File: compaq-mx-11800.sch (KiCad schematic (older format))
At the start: 246 parts

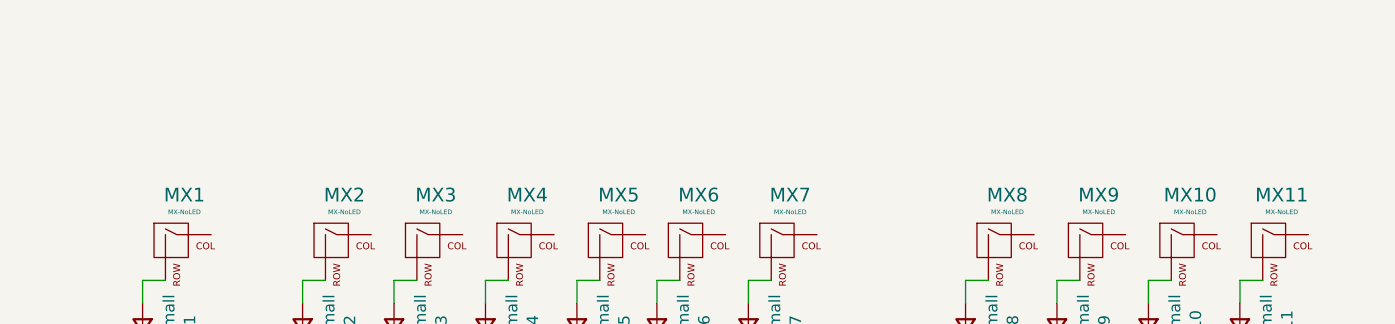
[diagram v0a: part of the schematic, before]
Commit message: add rest of the pcb mounting holes
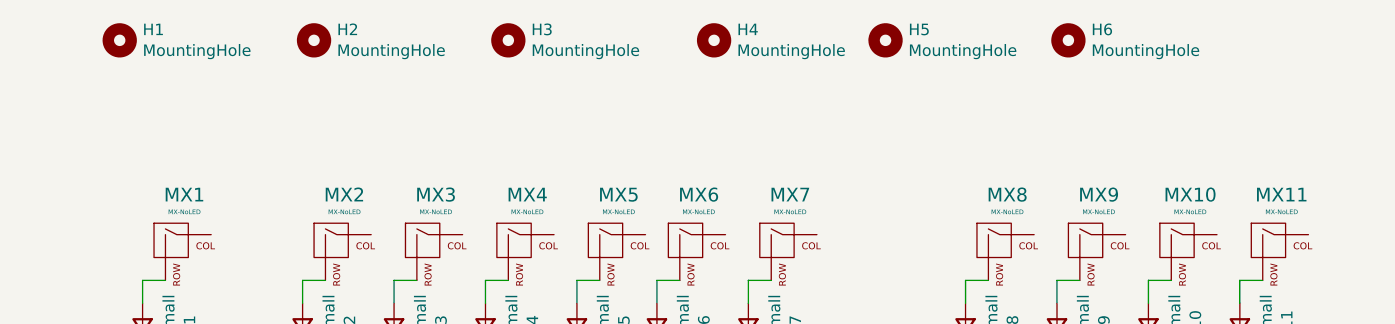
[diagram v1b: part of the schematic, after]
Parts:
- added H1, H2, H3, H4, H5: MountingHole, MountingHole:MountingHole_3.2mm_M3, symbol Mechanical:MountingHole
- added H6: MountingHole, Keebio-Parts:SolidCopper, symbol Mechanical:MountingHole
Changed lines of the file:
@@
+	1    0    0    -1
+$EndComp
+$Comp
+L Mechanical:MountingHole H1
+U 1 1 61C64BC8
+P 1000 100
+F 0 "H1" H 1100 146 50  0000 L CNN
+F 1 "MountingHole" H 1100 55  50  0000 L CNN
+F 2 "MountingHole:MountingHole_3.2mm_M3" H 1000 100 50  0001 C CNN
+F 3 "~" H 1000 100 50  0001 C CNN
+	1    1000 100
+	1    0    0    -1
+$EndComp
+$Comp
+L Mechanical:MountingHole H2
+U 1 1 61C9736A
+P 1850 100
+F 0 "H2" H 1950 146 50  0000 L CNN
+F 1 "MountingHole" H 1950 55  50  0000 L CNN
+F 2 "MountingHole:MountingHole_3.2mm_M3" H 1850 100 50  0001 C CNN
+F 3 "~" H 1850 100 50  0001 C CNN
+	1    1850 100
+	1    0    0    -1
+$EndComp
+$Comp
+L Mechanical:MountingHole H3
+U 1 1 61C97D62
+P 2700 100
+F 0 "H3" H 2800 146 50  0000 L CNN
+F 1 "MountingHole" H 2800 55  50  0000 L CNN
+F 2 "MountingHole:MountingHole_3.2mm_M3" H 2700 100 50  0001 C CNN
+F 3 "~" H 2700 100 50  0001 C CNN
+	1    2700 100
+	1    0    0    -1
+$EndComp
+$Comp
+L Mechanical:MountingHole H4
+U 1 1 61C98E0E
+P 3600 100
+F 0 "H4" H 3700 146 50  0000 L CNN
+F 1 "MountingHole" H 3700 55  50  0000 L CNN
+F 2 "MountingHole:MountingHole_3.2mm_M3" H 3600 100 50  0001 C CNN
+F 3 "~" H 3600 100 50  0001 C CNN
+	1    3600 100
+	1    0    0    -1
+$EndComp
+$Comp
+L Mechanical:MountingHole H5
+U 1 1 61CD4313
+P 4350 100
+F 0 "H5" H 4450 146 50  0000 L CNN
+F 1 "MountingHole" H 4450 55  50  0000 L CNN
+F 2 "MountingHole:MountingHole_3.2mm_M3" H 4350 100 50  0001 C CNN
+F 3 "~" H 4350 100 50  0001 C CNN
+	1    4350 100
+	1    0    0    -1
+$EndComp
+$Comp
+L Mechanical:MountingHole H6
+U 1 1 61D29BE7
+P 5150 100
+F 0 "H6" H 5250 146 50  0000 L CNN
+F 1 "MountingHole" H 5250 55  50  0000 L CNN
+F 2 "Keebio-Parts:SolidCopper" H 5150 100 50  0001 C CNN
+F 3 "~" H 5150 100 50  0001 C CNN
+	1    5150 100
 	1    0    0    -1
 $EndComp

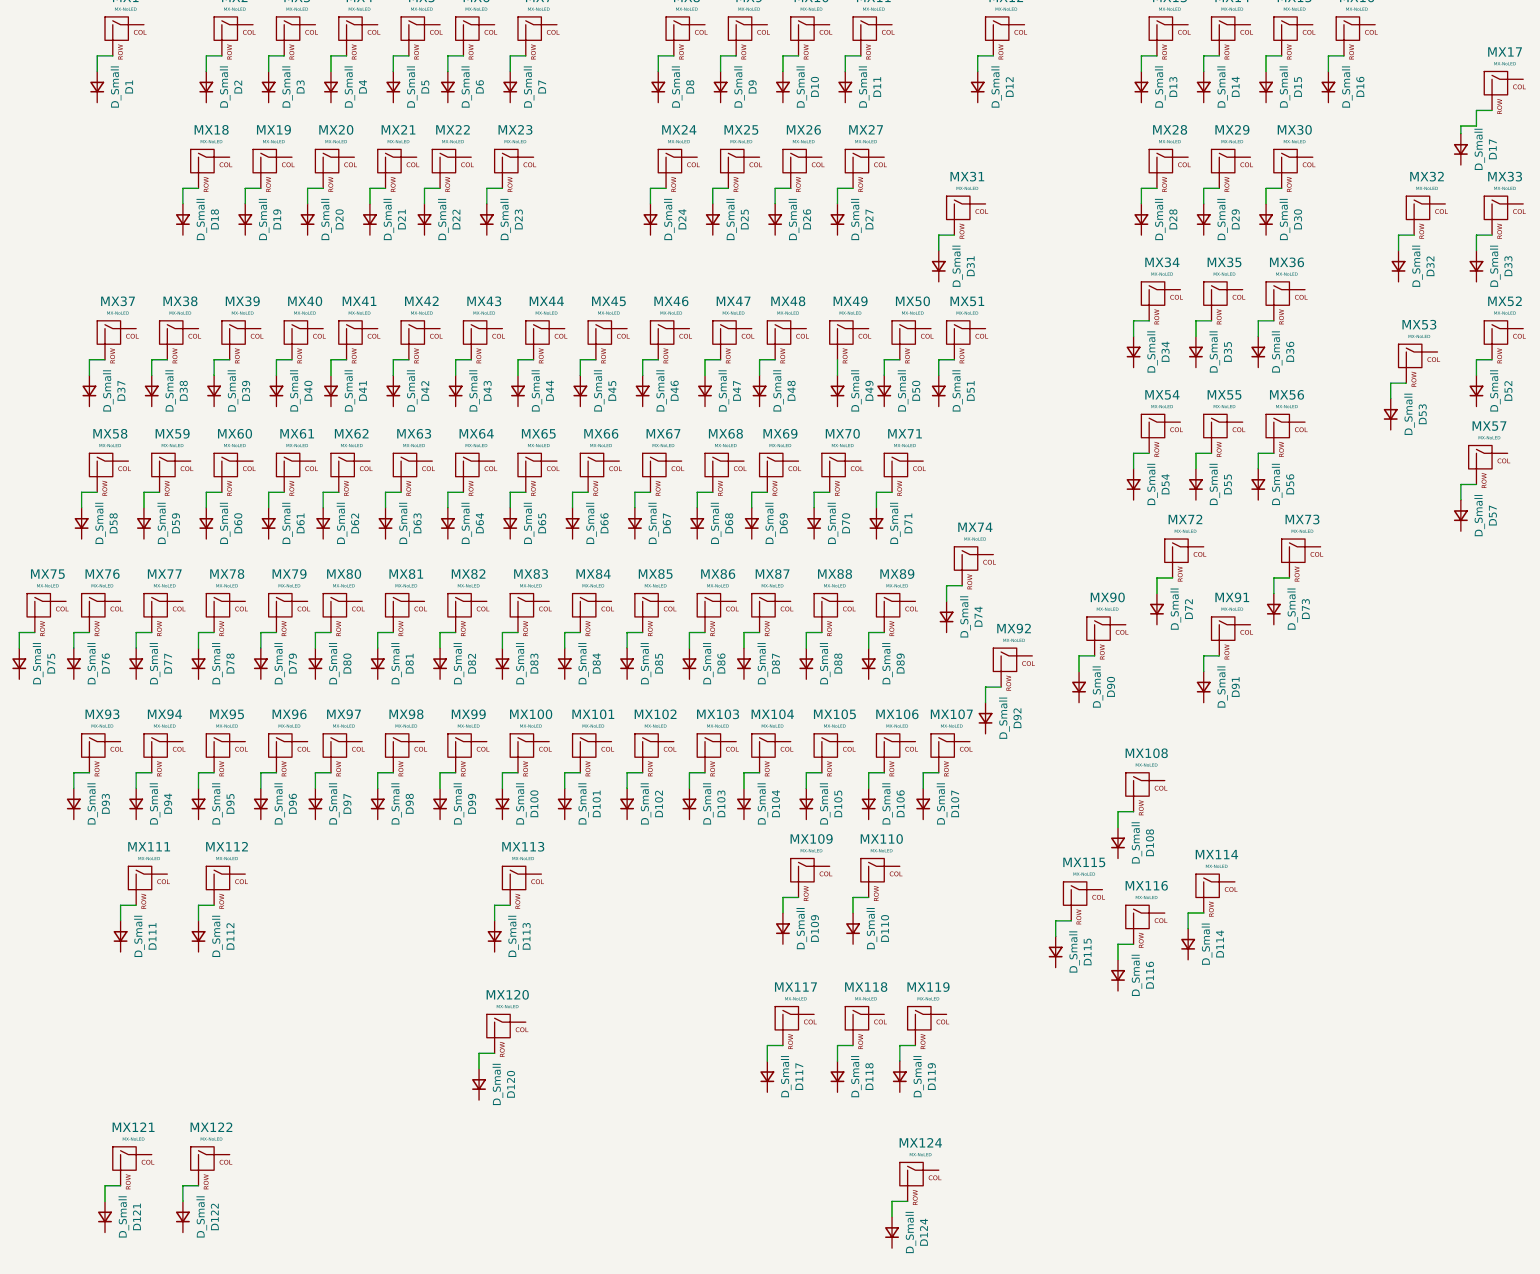
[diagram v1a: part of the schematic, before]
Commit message: remove extra diodes for multilayout
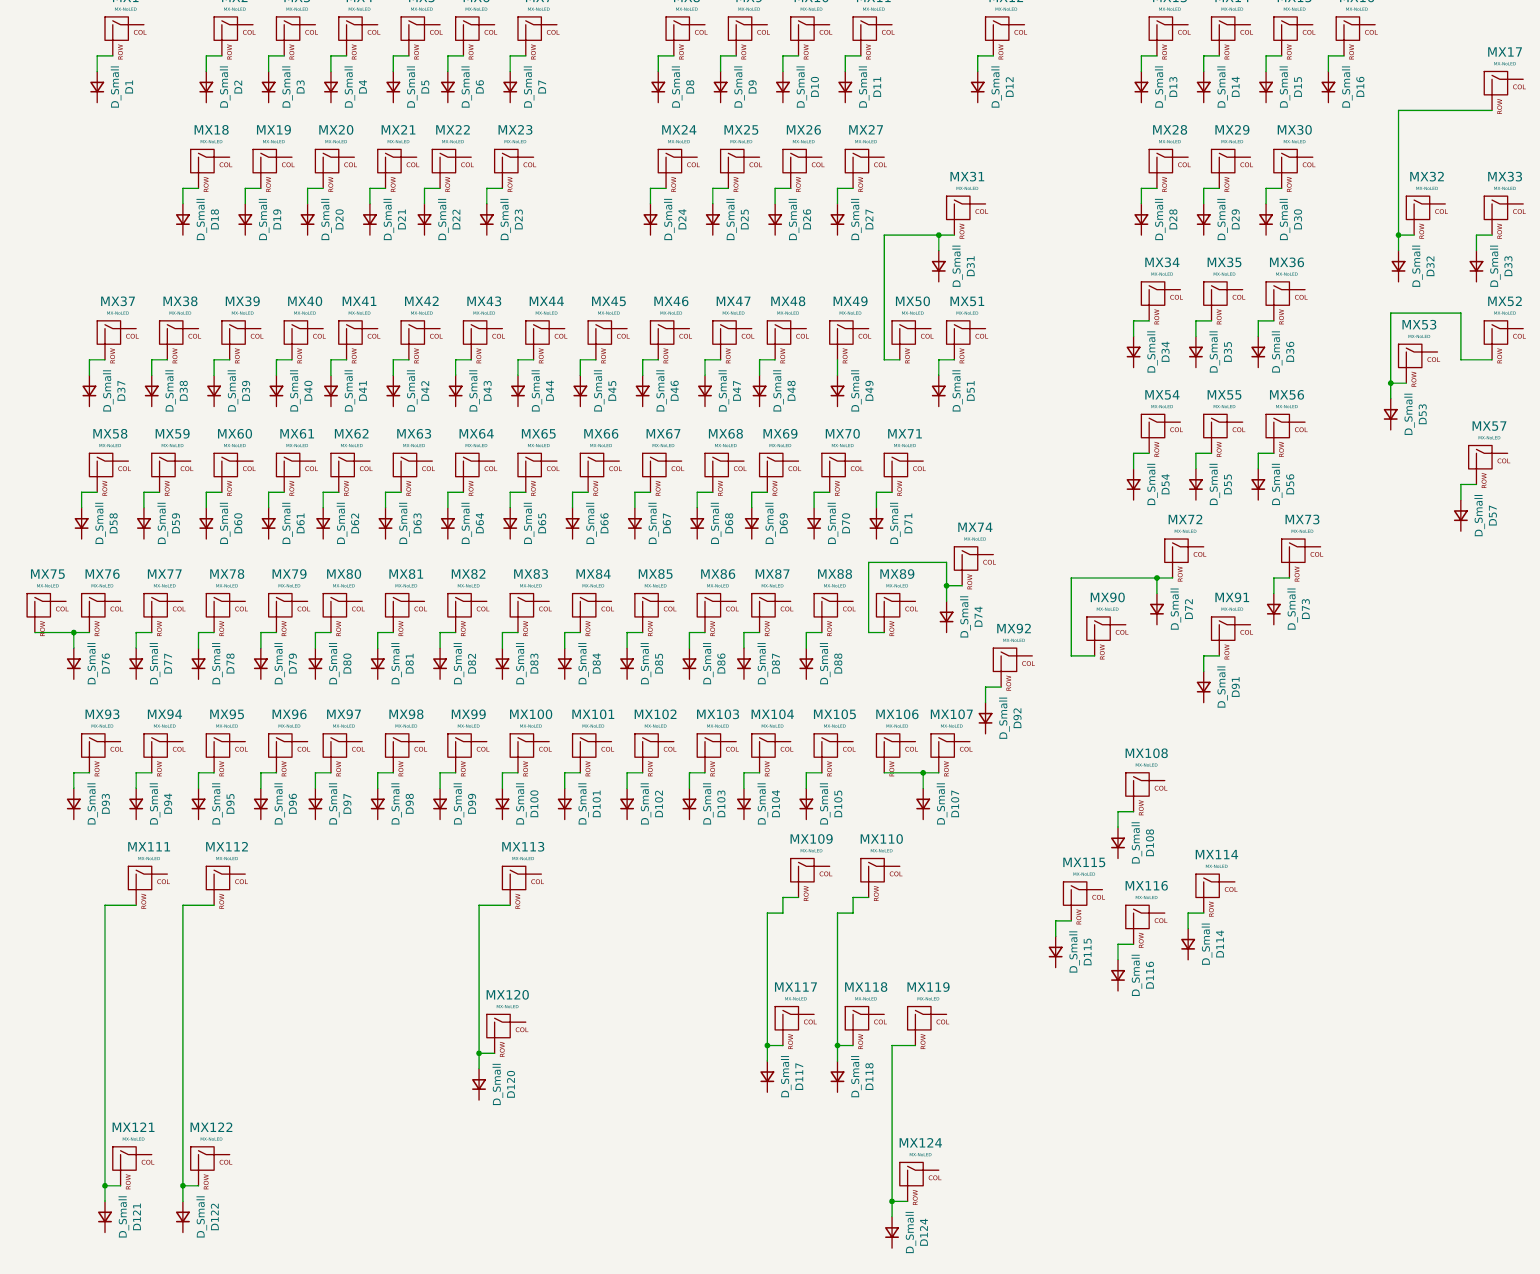
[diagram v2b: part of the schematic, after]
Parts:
- removed D106, D109, D110, D111, D112, D113, D119, D17, D50, D52, D75, D89, D90: D_Small, Keebio-Parts:Diode-dual, symbol Device:D_Small
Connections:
- net at D72.2 (A), MX72.2 (ROW): now also MX90.2 (ROW)
- net at D53.2 (A), MX53.2 (ROW): now also MX52.2 (ROW)
- net at D107.2 (A), MX107.2 (ROW): now also MX106.2 (ROW)
- net at D32.2 (A), MX32.2 (ROW): now also MX17.2 (ROW)
- net at MX50.2 (ROW): now also D31.2 (A), MX31.2 (ROW)
- net at D76.2 (A), MX76.2 (ROW): now also MX75.2 (ROW)
- net at MX89.2 (ROW): now also D74.2 (A), MX74.2 (ROW)
- net at MX111.2 (ROW): now also D121.2 (A), MX121.2 (ROW)
- net at MX112.2 (ROW): now also D122.2 (A), MX122.2 (ROW)
- net at MX113.2 (ROW): now also D120.2 (A), MX120.2 (ROW)
- net at MX109.2 (ROW): now also D117.2 (A), MX117.2 (ROW)
- net at MX110.2 (ROW): now also D118.2 (A), MX118.2 (ROW)
- net at MX119.2 (ROW): now also D124.2 (A), MX124.2 (ROW)
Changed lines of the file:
@@
 Wire Wire Line
 	1100 1150 1100 1250
-Wire Wire Line
-	6050 5750 6050 5850
-Wire Wire Line
-	6150 5750 6050 5750
-$Comp
-L Device:D_Small D106
-U 1 1 61D63EB3
-P 6050 5950
-F 0 "D106" H 6050 5743 50  0000 C CNN
-F 1 "D_Small" H 6050 5834 50  0000 C CNN
-F 2 "Keebio-Parts:Diode-dual" V 6050 5950 50  0001 C CNN
-F 3 "~" V 6050 5950 50  0001 C CNN
-	1    6050 5950
-	0    -1   -1   0
-$EndComp
 $Comp
 L MX_Alps_Hybrid:MX-NoLED MX106
@@
 $EndComp
 Wire Wire Line
-	6050 4850 6050 4950
-Wire Wire Line
 	6150 4850 6050 4850
 $Comp
-L Device:D_Small D89
-U 1 1 61CF77AA
-P 6050 5050
-F 0 "D89" H 6050 4843 50  0000 C CNN
-F 1 "D_Small" H 6050 4934 50  0000 C CNN
-F 2 "Keebio-Parts:Diode-dual" V 6050 5050 50  0001 C CNN
-F 3 "~" V 6050 5050 50  0001 C CNN
-	1    6050 5050
-	0    -1   -1   0
-$EndComp
-$Comp
 L MX_Alps_Hybrid:MX-NoLED MX89
 U 1 1 61CF77A4
@@
 	1    0    0    -1
 $EndComp
-Wire Wire Line
-	6150 3100 6150 3200
-Wire Wire Line
-	6250 3100 6150 3100
-$Comp
-L Device:D_Small D50
-U 1 1 61CC6202
-P 6150 3300
-F 0 "D50" H 6150 3093 50  0000 C CNN
-F 1 "D_Small" H 6150 3184 50  0000 C CNN
-F 2 "Keebio-Parts:Diode-dual" V 6150 3300 50  0001 C CNN
-F 3 "~" V 6150 3300 50  0001 C CNN
-	1    6150 3300
-	0    -1   -1   0
-$EndComp
 $Comp
 L MX_Alps_Hybrid:MX-NoLED MX50
@@
 	1    0    0    -1
 $EndComp
-Wire Wire Line
-	9950 1500 9950 1600
-Wire Wire Line
-	10050 1500 9950 1500
 $Comp
 L MX_Alps_Hybrid:MX-NoLED MX17
@@
 	1    0    0    -1
 $EndComp
-Wire Wire Line
-	9950 3100 9950 3200
-Wire Wire Line
-	10050 3100 9950 3100
-$Comp
-L Device:D_Small D52
-U 1 1 61C8E93E
-P 9950 3300
-F 0 "D52" H 9950 3093 50  0000 C CNN
-F 1 "D_Small" H 9950 3184 50  0000 C CNN
-F 2 "Keebio-Parts:Diode-dual" V 9950 3300 50  0001 C CNN
-F 3 "~" V 9950 3300 50  0001 C CNN
-	1    9950 3300
-	0    -1   -1   0
-$EndComp
 $Comp
 L MX_Alps_Hybrid:MX-NoLED MX52
@@
 	1    0    0    -1
 $EndComp
-Wire Wire Line
-	7400 5000 7400 5100
-Wire Wire Line
-	7500 5000 7400 5000
-$Comp
-L Device:D_Small D90
-U 1 1 61C8491A
-P 7400 5200
-F 0 "D90" H 7400 4993 50  0000 C CNN
-F 1 "D_Small" H 7400 5084 50  0000 C CNN
-F 2 "Keebio-Parts:Diode-dual" V 7400 5200 50  0001 C CNN
-F 3 "~" V 7400 5200 50  0001 C CNN
-	1    7400 5200
-	0    -1   -1   0
-$EndComp
 $Comp
 L MX_Alps_Hybrid:MX-NoLED MX90
@@
 	1    0    0    -1
 $EndComp
-Wire Wire Line
-	9950 1600 9850 1600
-$Comp
-L Device:D_Small D17
-U 1 1 61DE22D7
-P 9850 1750
-F 0 "D17" H 9850 1543 50  0000 C CNN
-F 1 "D_Small" H 9850 1634 50  0000 C CNN
-F 2 "Keebio-Parts:Diode-dual" V 9850 1750 50  0001 C CNN
-F 3 "~" V 9850 1750 50  0001 C CNN
-	1    9850 1750
-	0    -1   -1   0
-$EndComp
-Wire Wire Line
-	9850 1600 9850 1650
 $Comp
 L Device:D_Small D49
@@
 Wire Wire Line
 	6500 2300 6500 2400
-Wire Wire Line
-	600  4850 600  4950
-Wire Wire Line
-	700  4850 600  4850
-$Comp
-L Device:D_Small D75
-U 1 1 61F8FFCC
-P 600 5050
-F 0 "D75" H 600 4843 50  0000 C CNN
-F 1 "D_Small" H 600 4934 50  0000 C CNN
-F 2 "Keebio-Parts:Diode-dual" V 600 5050 50  0001 C CNN
-F 3 "~" V 600 5050 50  0001 C CNN
-	1    600  5050
-	0    -1   -1   0
-$EndComp
 $Comp
 L MX_Alps_Hybrid:MX-NoLED MX75
@@
 	1    0    0    -1
 $EndComp
-Wire Wire Line
-	1250 6600 1250 6700
-Wire Wire Line
-	1350 6600 1250 6600
-$Comp
-L Device:D_Small D111
-U 1 1 61DEDDFC
-P 1250 6800
-F 0 "D111" H 1250 6593 50  0000 C CNN
-F 1 "D_Small" H 1250 6684 50  0000 C CNN
-F 2 "Keebio-Parts:Diode-dual" V 1250 6800 50  0001 C CNN
-F 3 "~" V 1250 6800 50  0001 C CNN
-	1    1250 6800
-	0    -1   -1   0
-$EndComp
 $Comp
 L MX_Alps_Hybrid:MX-NoLED MX111
@@
 	1    0    0    -1
 $EndComp
-Wire Wire Line
-	1750 6600 1750 6700
-Wire Wire Line
-	1850 6600 1750 6600
-$Comp
-L Device:D_Small D112
-U 1 1 61DFB6FC
-P 1750 6800
-F 0 "D112" H 1750 6593 50  0000 C CNN
-F 1 "D_Small" H 1750 6684 50  0000 C CNN
-F 2 "Keebio-Parts:Diode-dual" V 1750 6800 50  0001 C CNN
-F 3 "~" V 1750 6800 50  0001 C CNN
-	1    1750 6800
-	0    -1   -1   0
-$EndComp
 $Comp
 L MX_Alps_Hybrid:MX-NoLED MX112
@@
 	1    0    0    -1
 $EndComp
-Wire Wire Line
-	3650 6600 3650 6700
-Wire Wire Line
-	3750 6600 3650 6600
-$Comp
-L Device:D_Small D113
-U 1 1 61E0971A
-P 3650 6800
-F 0 "D113" H 3650 6593 50  0000 C CNN
-F 1 "D_Small" H 3650 6684 50  0000 C CNN
-F 2 "Keebio-Parts:Diode-dual" V 3650 6800 50  0001 C CNN
-F 3 "~" V 3650 6800 50  0001 C CNN
-	1    3650 6800
-	0    -1   -1   0
-$EndComp
 $Comp
 L MX_Alps_Hybrid:MX-NoLED MX113
@@
 	5600 6550 5500 6550
 $Comp
-L Device:D_Small D109
-U 1 1 61E178E0
-P 5500 6750
-F 0 "D109" H 5500 6543 50  0000 C CNN
-F 1 "D_Small" H 5500 6634 50  0000 C CNN
-F 2 "Keebio-Parts:Diode-dual" V 5500 6750 50  0001 C CNN
-F 3 "~" V 5500 6750 50  0001 C CNN
-	1    5500 6750
-	0    -1   -1   0
-$EndComp
-$Comp
 L MX_Alps_Hybrid:MX-NoLED MX109
 U 1 1 61E178E6
@@
 	6050 6550 5950 6550
 $Comp
-L Device:D_Small D110
-U 1 1 61E25C7E
-P 5950 6750
-F 0 "D110" H 5950 6543 50  0000 C CNN
-F 1 "D_Small" H 5950 6634 50  0000 C CNN
-F 2 "Keebio-Parts:Diode-dual" V 5950 6750 50  0001 C CNN
-F 3 "~" V 5950 6750 50  0001 C CNN
-	1    5950 6750
-	0    -1   -1   0
-$EndComp
-$Comp
 L MX_Alps_Hybrid:MX-NoLED MX110
 U 1 1 61E25C84
@@
 $EndComp
 Wire Wire Line
-	3550 7550 3550 7650
-Wire Wire Line
 	3650 7550 3550 7550
 $Comp
@@
 $EndComp
 Wire Wire Line
-	5400 7500 5400 7600
-Wire Wire Line
 	5500 7500 5400 7500
 $Comp
@@
 	1    0    0    -1
 $EndComp
-Wire Wire Line
-	6250 7500 6250 7600
-Wire Wire Line
-	6350 7500 6250 7500
-$Comp
-L Device:D_Small D119
-U 1 1 61ED7E77
-P 6250 7700
-F 0 "D119" H 6250 7493 50  0000 C CNN
-F 1 "D_Small" H 6250 7584 50  0000 C CNN
-F 2 "Keebio-Parts:Diode-dual" V 6250 7700 50  0001 C CNN
-F 3 "~" V 6250 7700 50  0001 C CNN
-	1    6250 7700
-	0    -1   -1   0
-$EndComp
 $Comp
 L MX_Alps_Hybrid:MX-NoLED MX119
@@
 	1    0    0    -1
 $EndComp
+Wire Wire Line
+	6250 3100 6150 3100
+Wire Wire Line
+	6150 3100 6150 2300
+Wire Wire Line
+	6150 2300 6500 2300
+Connection ~ 6500 2300
+Wire Wire Line
+	10050 1500 9450 1500
+Wire Wire Line
+	9450 1500 9450 2300
+Connection ~ 9450 2300
+Wire Wire Line
+	10050 3100 9850 3100
+Wire Wire Line
+	9850 3100 9850 2800
+Wire Wire Line
+	9850 2800 9400 2800
+Wire Wire Line
+	9400 2800 9400 3250
+Connection ~ 9400 3250
+Wire Wire Line
+	7500 5000 7350 5000
+Wire Wire Line
+	7350 5000 7350 4500
+Wire Wire Line
+	7350 4500 7900 4500
+Connection ~ 7900 4500
+Wire Wire Line
+	700  4850 950  4850
+Connection ~ 950  4850
+Wire Wire Line
+	6050 4850 6050 4400
+Wire Wire Line
+	6050 4400 6550 4400
+Wire Wire Line
+	6550 4400 6550 4550
+Connection ~ 6550 4550
+Wire Wire Line
+	6150 5750 6400 5750
+Connection ~ 6400 5750
+Wire Wire Line
+	1150 6600 1150 8400
+Wire Wire Line
+	1150 6600 1350 6600
+Connection ~ 1150 8400
+Wire Wire Line
+	1650 6600 1650 8400
+Connection ~ 1650 8400
+Wire Wire Line
+	1650 6600 1850 6600
+Wire Wire Line
+	3550 6600 3750 6600
+Wire Wire Line
+	3550 6600 3550 7550
+Connection ~ 3550 7550
+Wire Wire Line
+	3550 7550 3550 7650
+Wire Wire Line
+	5500 6650 5400 6650
+Wire Wire Line
+	5400 6650 5400 7500
+Connection ~ 5400 7500
+Wire Wire Line
+	5400 7500 5400 7600
+Wire Wire Line
+	5950 6650 5850 6650
+Wire Wire Line
+	5850 6650 5850 7500
+Connection ~ 5850 7500
+Wire Wire Line
+	6200 7500 6200 8500
+Wire Wire Line
+	6200 7500 6350 7500
+Connection ~ 6200 8500
 $EndSCHEMATC

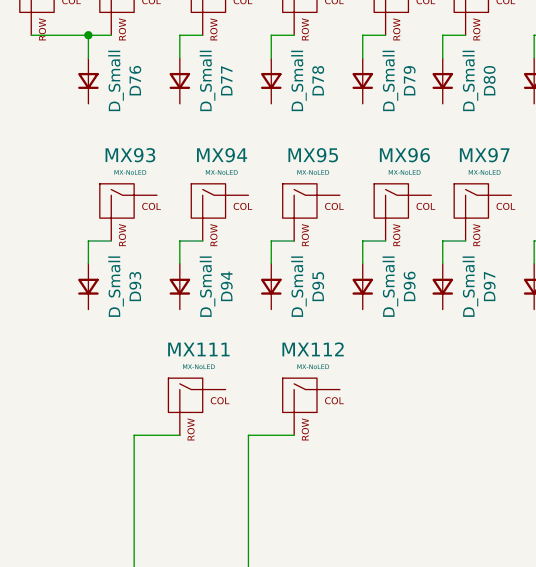
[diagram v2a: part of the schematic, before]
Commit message: connect diodes - frow
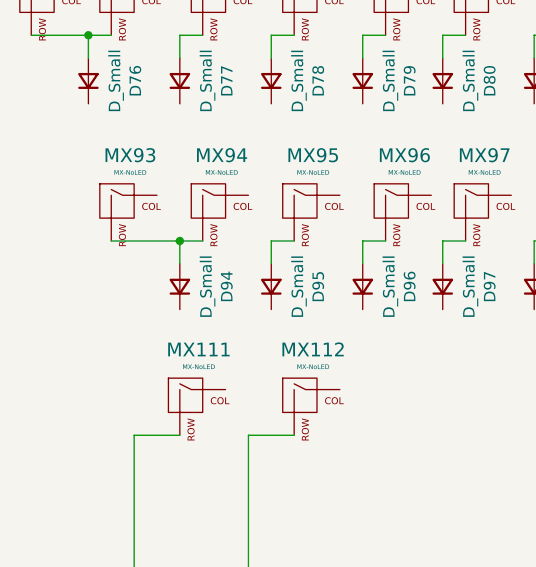
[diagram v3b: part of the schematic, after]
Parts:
- removed D93: D_Small, Keebio-Parts:Diode-dual, symbol Device:D_Small
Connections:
- net at MX93.2 (ROW): now also D94.2 (A), MX94.2 (ROW)
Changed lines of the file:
@@
 	1    0    0    -1
-$EndComp
-Wire Wire Line
-	950  5750 950  5850
-Wire Wire Line
-	1050 5750 950  5750
-$Comp
-L Device:D_Small D93
-U 1 1 61D63DFD
-P 950 5950
-F 0 "D93" H 950 5743 50  0000 C CNN
-F 1 "D_Small" H 950 5834 50  0000 C CNN
-F 2 "Keebio-Parts:Diode-dual" V 950 5950 50  0001 C CNN
-F 3 "~" V 950 5950 50  0001 C CNN
-	1    950  5950
-	0    -1   -1   0
 $EndComp
 $Comp
@@
 	6200 7500 6350 7500
 Connection ~ 6200 8500
+Wire Wire Line
+	1050 5750 1350 5750
+Connection ~ 1350 5750
 $EndSCHEMATC

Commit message: connect rows and columns in .sch
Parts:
- renumbered MX15 to MX_*, MX16 to MX_-, MX14 to MX_/, MX28 to MX_7, MX32 to MX_P+, MX73 to MX_P,, MX72 to MX_P0, MX54 to MX_P1, MX55 to MX_P2, MX56 to MX_P3, MX34 to MX_P4, MX35 to MX_P5, MX36 to MX_P6, MX29 to MX_P8, MX30 to MX_P9, MX53 to MX_Penter, MX13 to MX_numlock
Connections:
- wire segments 252 -> 723
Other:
- moved on the sheet: D1, D10, D100, D101, D102, D103, D104, D105, D107, D108, D11, D114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
